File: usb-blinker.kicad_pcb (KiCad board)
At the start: 2 copper layers, 30 x 25 mm, 11 parts, among them J1 USB_C_Receptacle_PowerOnly_6P, U1 TLC555xPW

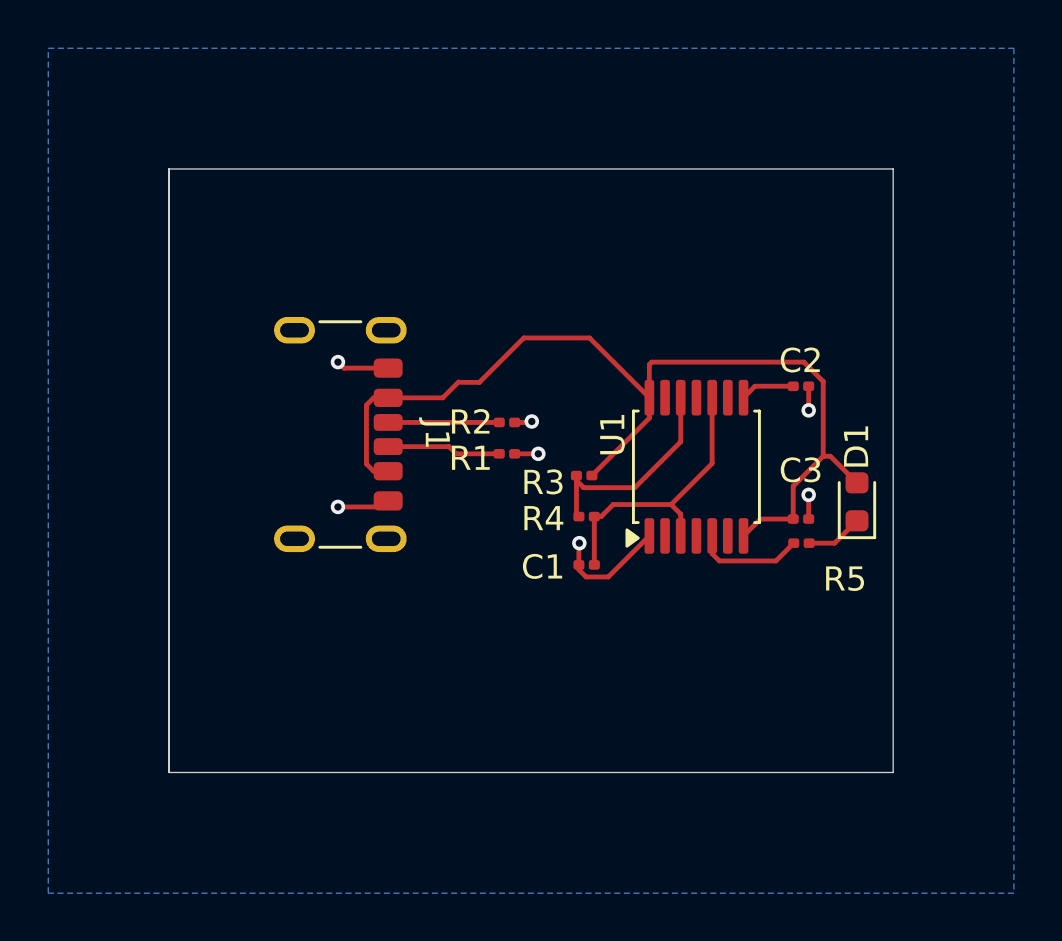
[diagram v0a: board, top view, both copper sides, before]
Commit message: added fuse, pcb remake
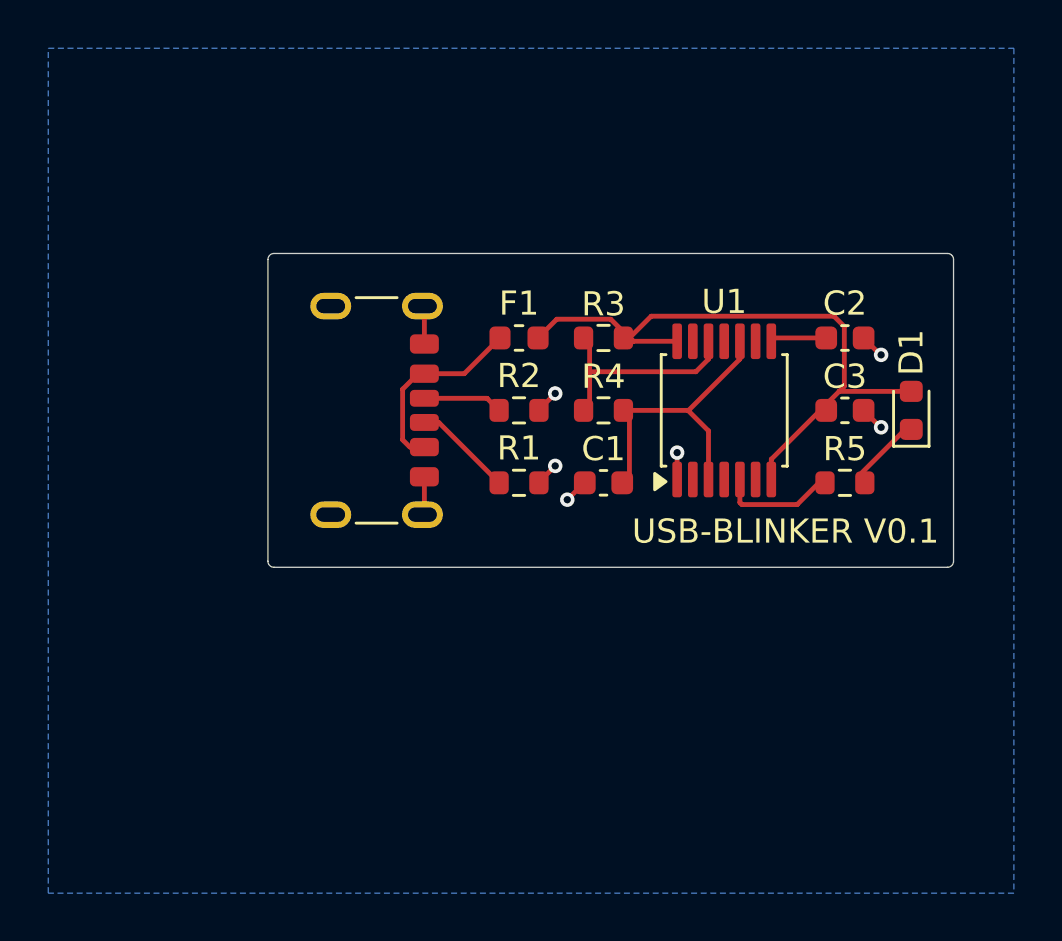
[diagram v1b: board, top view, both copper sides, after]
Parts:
- added F1: 500mA, Fuse:Fuse_0603_1608Metric, F.Cu at (139.5, 87.0)
- C1, C2, C3: footprint Capacitor_SMD:C_0201_0603Metric -> Capacitor_SMD:C_0603_1608Metric
- R1, R2, R3, R4, R5: footprint Resistor_SMD:R_0201_0603Metric -> Resistor_SMD:R_0603_1608Metric
- moved R3 5.76 mm to (143.0, 87.0)
- moved C3 4.85 mm to (153.0, 90.0)
- moved R4 4.46 mm to (143.0, 90.0)
- moved D1 4.41 mm to (155.8, 90.0)
- moved C1 3.47 mm to (143.0, 93.0)
- moved R5 3.08 mm to (153.0, 93.0)
- moved C2 2.70 mm to (153.0, 87.0)
- moved U1 2.61 mm to (148.0, 90.0)
- moved J1 1.80 mm to (132.5, 90.0)
- moved R1 1.30 mm to (139.5, 93.0)
- moved R2 0.71 mm to (139.5, 90.0)
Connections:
- J1 pad A9: +5V -> Net-(F1-Pad1)
- J1 pad B9: +5V -> Net-(F1-Pad1)
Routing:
- net +5V: track 40.8 -> 26.6 mm
- net Net-(F1-Pad1): track 0.00 -> 8.35 mm
- net 0: track 12.9 -> 10.1 mm, vias 7 -> 6
- net Net-(U1-THRES): track 12.0 -> 13.0 mm
- net Net-(D1-K): track 2.36 -> 3.36 mm
- net Net-(J1-CC1): track 4.60 -> 3.66 mm
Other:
- board size 30 x 25 mm -> 28.4 x 13 mm
- board text added: "USB-BLINKER V0.1"

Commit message: wider power traces
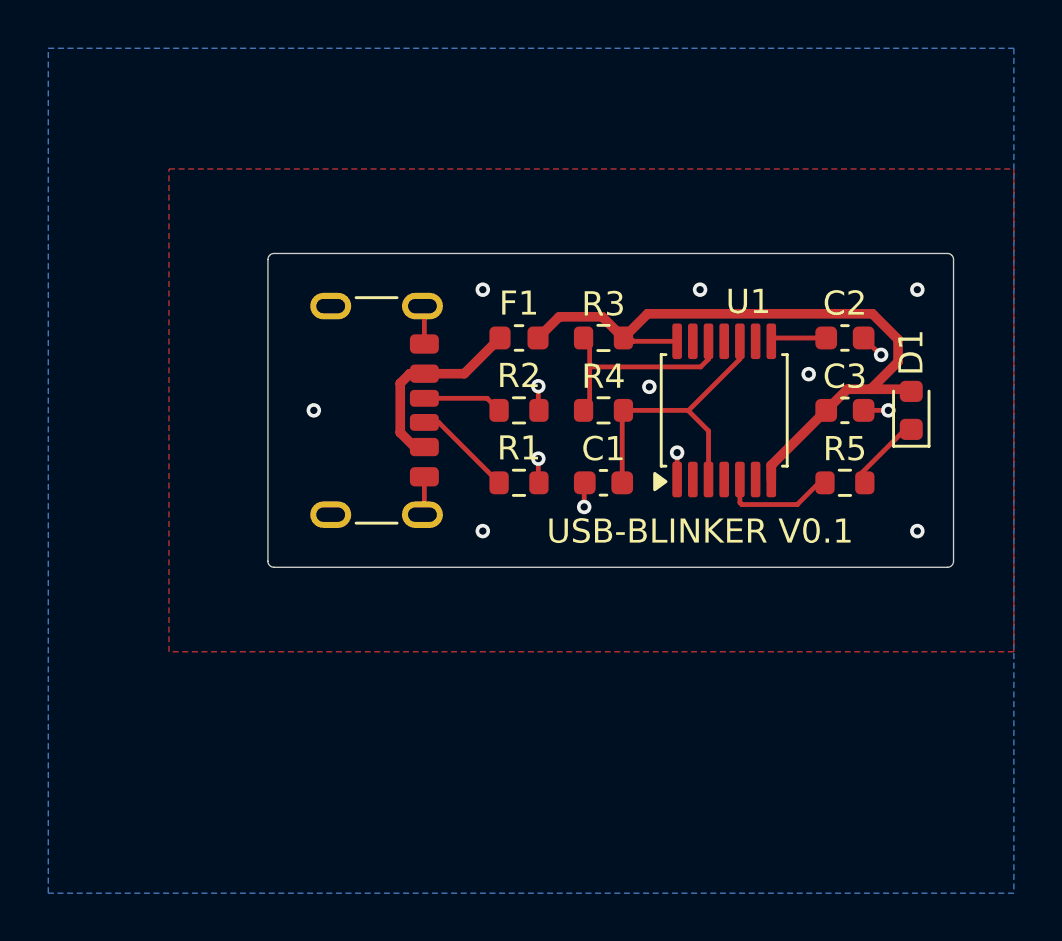
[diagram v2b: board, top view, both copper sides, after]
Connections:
- net Net-(F1-Pad1) renamed VBUS
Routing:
- net +5V: track 26.6 -> 29.3 mm
- net 0: track 10.1 -> 10.5 mm, vias 6 -> 14
- added copper zone on F.Cu, net 0
